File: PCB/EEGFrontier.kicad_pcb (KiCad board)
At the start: 2 copper layers, 55 x 41.5 mm, 33 parts, among them J1 Conn_01x08_Pin, SW1 SW_Push, U1 102010428, U2 ADS1299-4PAGR

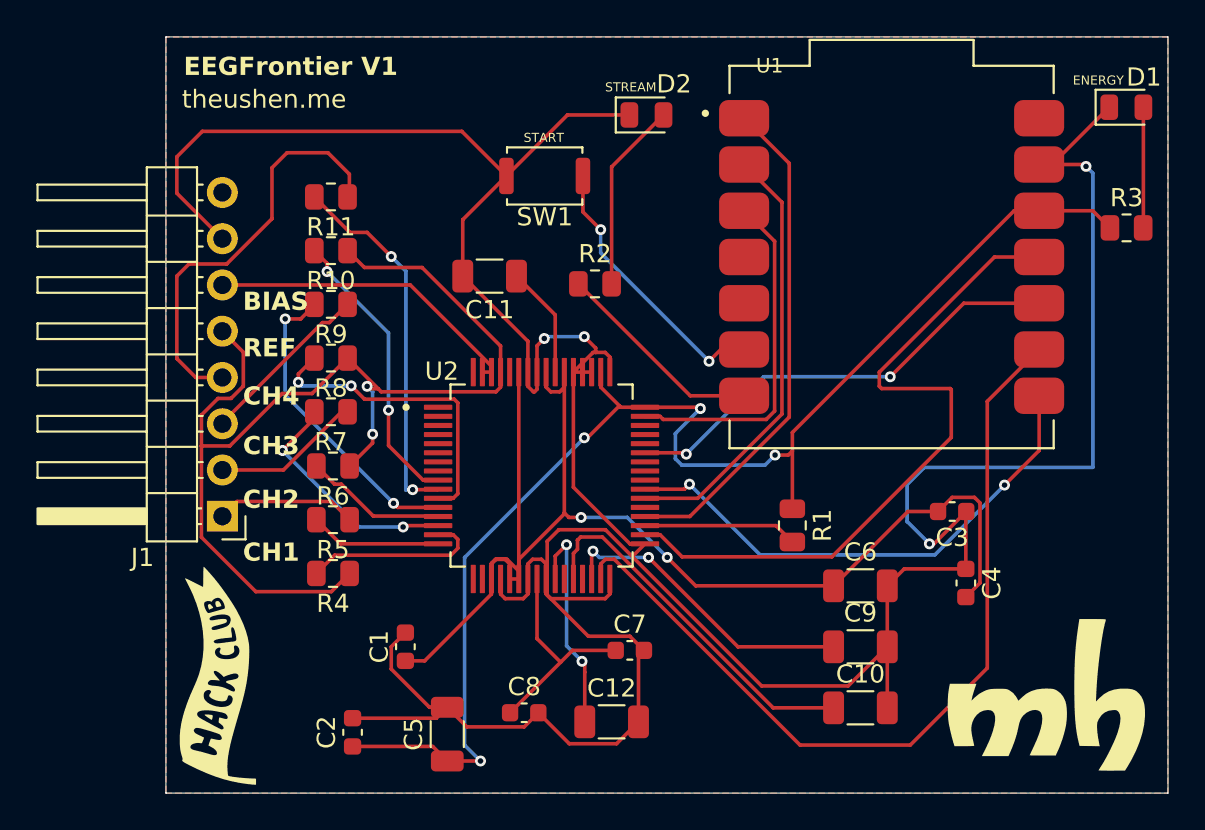
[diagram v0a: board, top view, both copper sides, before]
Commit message: Critical: Fixed float 3V3 #5
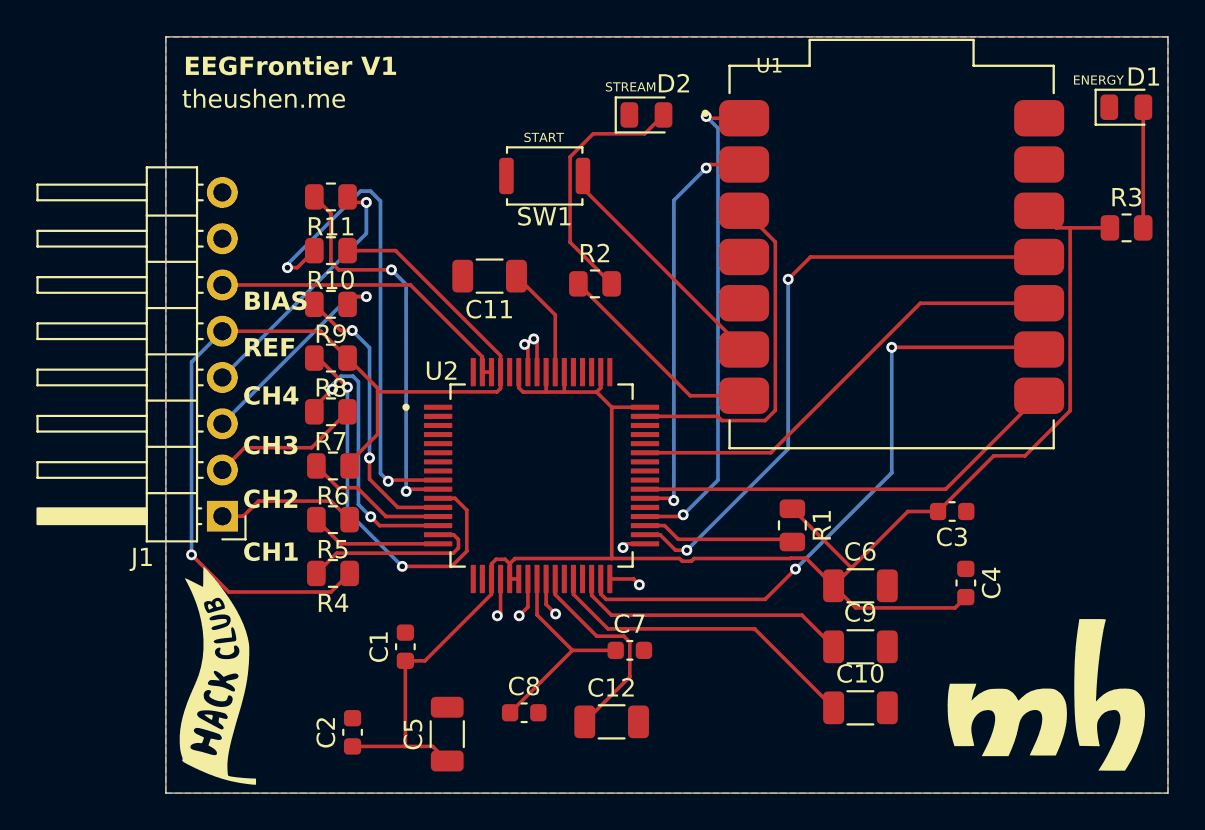
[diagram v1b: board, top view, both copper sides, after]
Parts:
- renumbered G*** to G1, G*** to G2, G*** to G4, G*** to G5
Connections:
- C1 pad 1: 3V3_A -> 3V3_D
- C3 pad 2: 3V3_A -> 3V3_D
- C4 pad 2: 3V3_A -> 3V3_D
- C6 pad 1: 3V3_A -> 3V3_D
- U2 pad 19: 3V3_A -> 3V3_D
- U2 pad 21: 3V3_A -> 3V3_D
- U2 pad 22: 3V3_A -> 3V3_D
- U2 pad 54: 3V3_A -> 3V3_D
- U2 pad 56: 3V3_A -> 3V3_D
- U2 pad 59: 3V3_A -> 3V3_D
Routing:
- net GND: track 200.2 -> 13.0 mm, vias 4 -> 7
- net 3V3_A: track 72.3 -> 0.00 mm, vias 2 -> 0
- net 3V3_D: track 74.9 -> 103.2 mm, vias 4 -> 0
- net SPI_SCK: track 46.8 -> 34.8 mm, vias 0 -> 2
- net Net-(U2-IN4N): track 15.9 -> 27.4 mm
- net EEG_CH4: track 23.2 -> 14.0 mm, vias 0 -> 1
- net SPI_CS: track 28.7 -> 23.8 mm, vias 2 -> 0
- net SPI_MOSI: track 38.9 -> 34.1 mm, vias 0 -> 2
- net Net-(U2-IN3N): track 17.1 -> 21.6 mm
- net EEG_REF: track 60.8 -> 57.1 mm, vias 2 -> 1
- net Net-(D2-A): track 10.5 -> 14.0 mm
- net Net-(U2-VCAP1): track 20.2 -> 17.7 mm
- net EEG_CH3: track 9.62 -> 12.0 mm, vias 0 -> 1
- net Net-(U2-IN2P): track 13.2 -> 15.2 mm
- net BTN_START: track 15.2 -> 13.2 mm, vias 2 -> 0
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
